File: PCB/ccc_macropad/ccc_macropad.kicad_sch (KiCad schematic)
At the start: 14 parts, among them SW1 SW_Push, SW2 SW_Push, SW3 SW_Push, SW4 SW_Push, SW5 SW_Push, SW6 SW_Push, U1 XIAO-RP2040-DIP

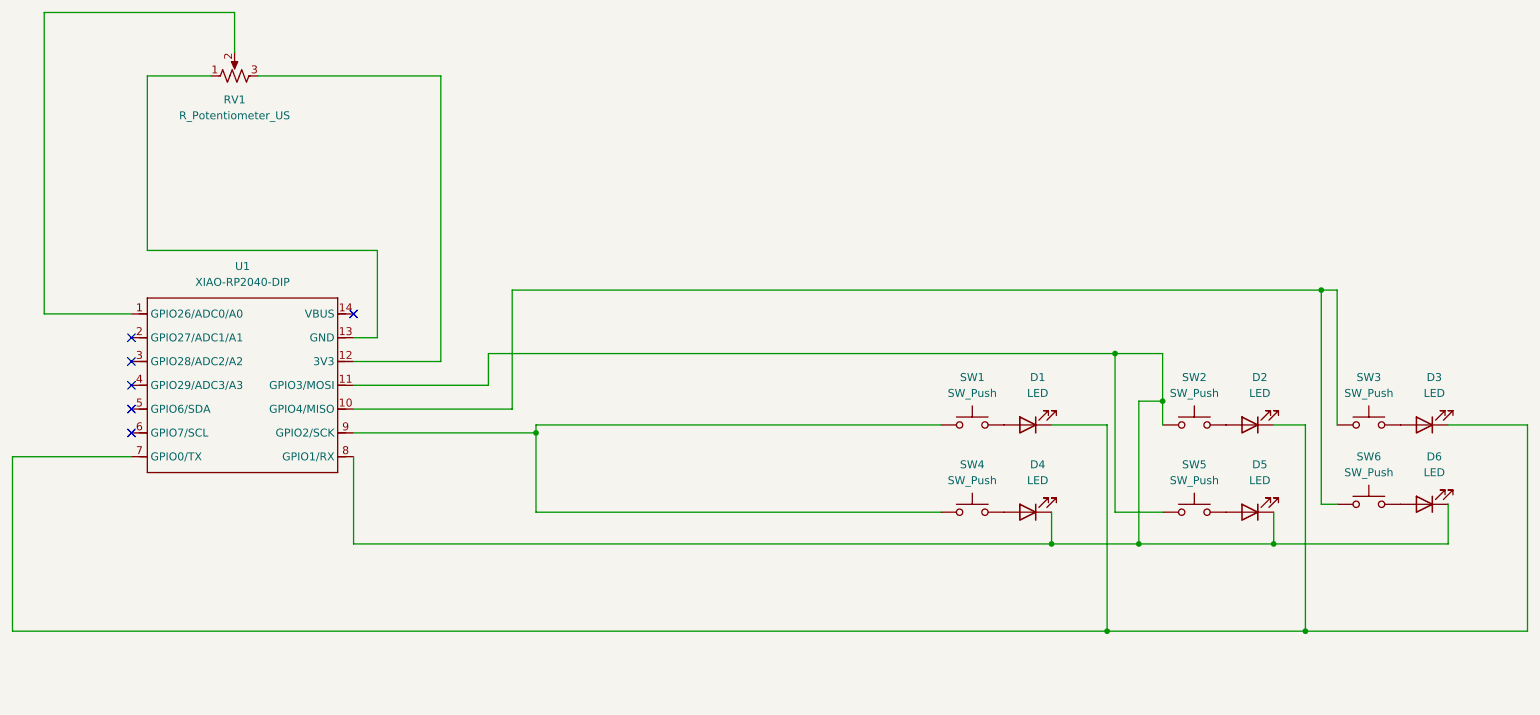
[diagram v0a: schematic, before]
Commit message: macropad:feature: add LED's and footprints
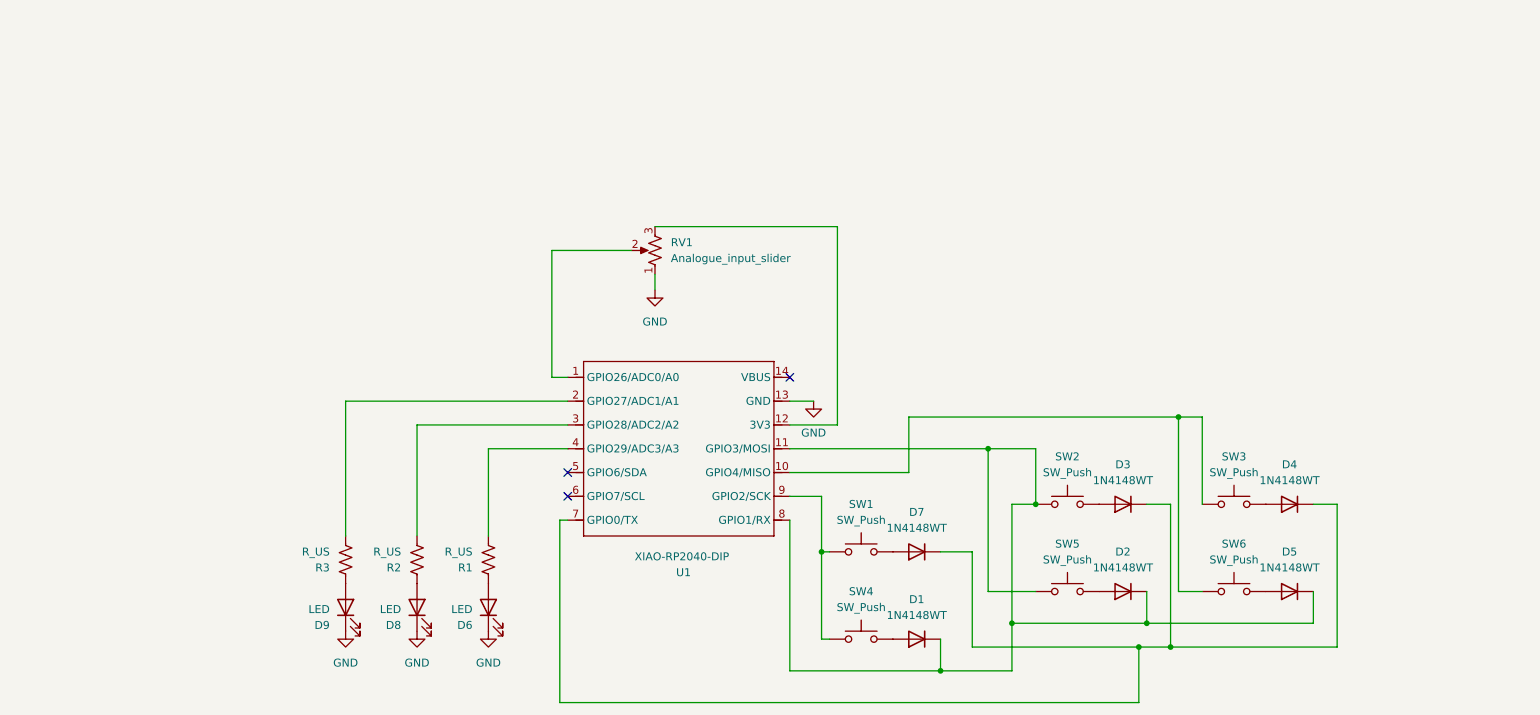
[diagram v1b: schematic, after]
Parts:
- removed D1, D2, D3, D4, D5: LED, symbol Device:LED
- added D1, D2, D3, D4, D5, D7: 1N4148WT, Diode_SMD:D_SOD-523, symbol Diode:1N4148WT
- added D8, D9: LED, symbol Device:LED
- added R1, R2, R3: R_US, symbol Device:R_US
- RV1: value R_Potentiometer_US -> Analogue_input_slider; footprint (none) -> Potentiometer_THT:Potentiometer_Bourns_PTA4543_Single_Slide
- SW1, SW2, SW3, SW4, SW5, SW6: footprint (none) -> Button_Switch_Keyboard:SW_Cherry_MX_1.00u_PCB
- U1: footprint Module:MOUDLE14P-XIAO-DIP-SMD -> XIAO Seeduino:XIAO-RP2040-DIP
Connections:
- net at U1.7 (GPIO0/TX): now also D3.1 (K), D4.1 (K), D7.1 (K)
- net at SW2.2: now also D3.2 (A)
- net at SW1.2: now also D7.2 (A)
- net at SW2.1, SW5.1, U1.11 (GPIO3/MOSI)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: now also D1.1 (K), D2.1 (K), D5.1 (K); no longer D6.1 (K)
- net at SW5.2: now also D2.2 (A)
- net GND: now reaches RV1.1, U1.13 (GND)
- net GND: now also D6.1 (K), D8.1 (K), D9.1 (K)
- net at U1.2 (GPIO27/ADC1/A1): now also R3.2
- net at U1.3 (GPIO28/ADC2/A2): now also R2.2
- net at U1.4 (GPIO29/ADC3/A3): now also R1.2
- net at SW4.2: now also D1.2 (A)
- net at D6.2 (A): now also R1.1; no longer SW6.2
- net at SW3.2: now also D4.2 (A)
- new net: D8.2 (A), R2.1
- new net: D9.2 (A), R3.1
- new net: D5.2 (A), SW6.2
- no-connect marks 6 -> 3
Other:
- moved on the sheet: RV1, SW1, SW2, SW3, SW4, SW5, SW6, U1
